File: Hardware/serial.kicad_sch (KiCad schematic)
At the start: 4 parts, among them J7 DG250-3-5-04P-11-00AH, U11 ISO7221

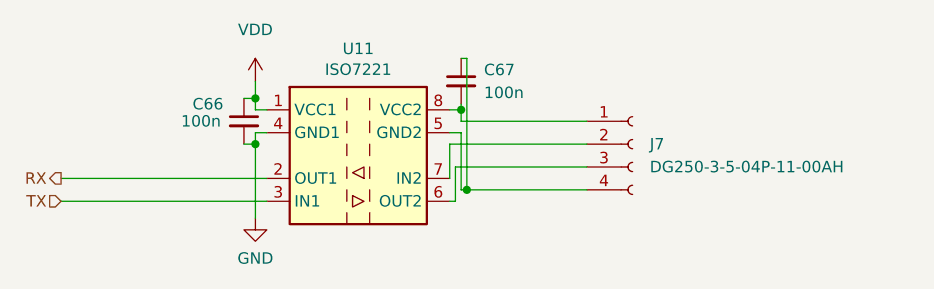
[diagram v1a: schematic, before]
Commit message: Toolchain set. Timer module added. Schematic files migrated.
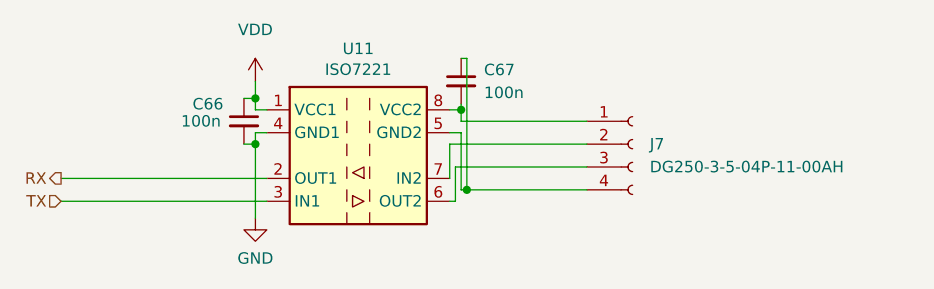
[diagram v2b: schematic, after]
